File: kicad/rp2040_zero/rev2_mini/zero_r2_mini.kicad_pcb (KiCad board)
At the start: 2 copper layers, 34.6 x 28.3 mm, 15 parts, among them J3 Debug port, J5 Debug port, Q1 DMG2302U, U1 RP2040-Zero

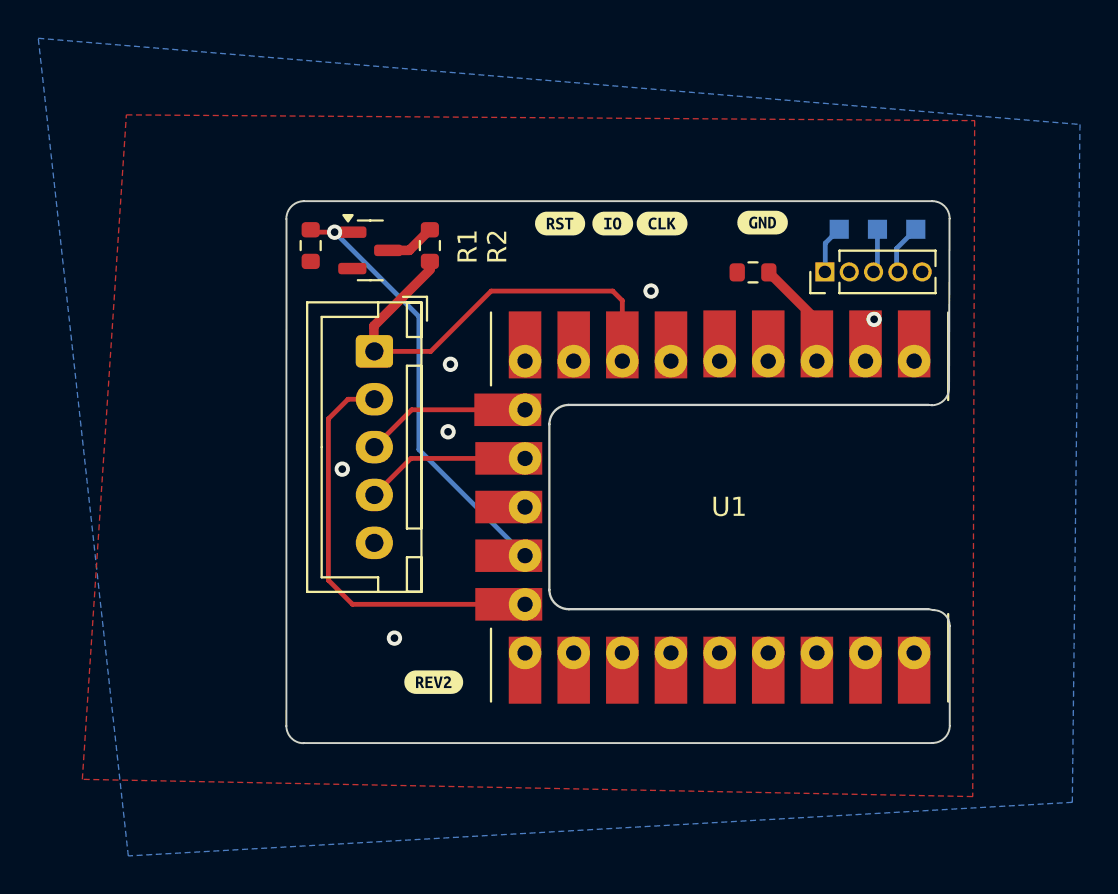
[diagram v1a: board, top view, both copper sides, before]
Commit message: kicad: add pullup resistor on rp2040
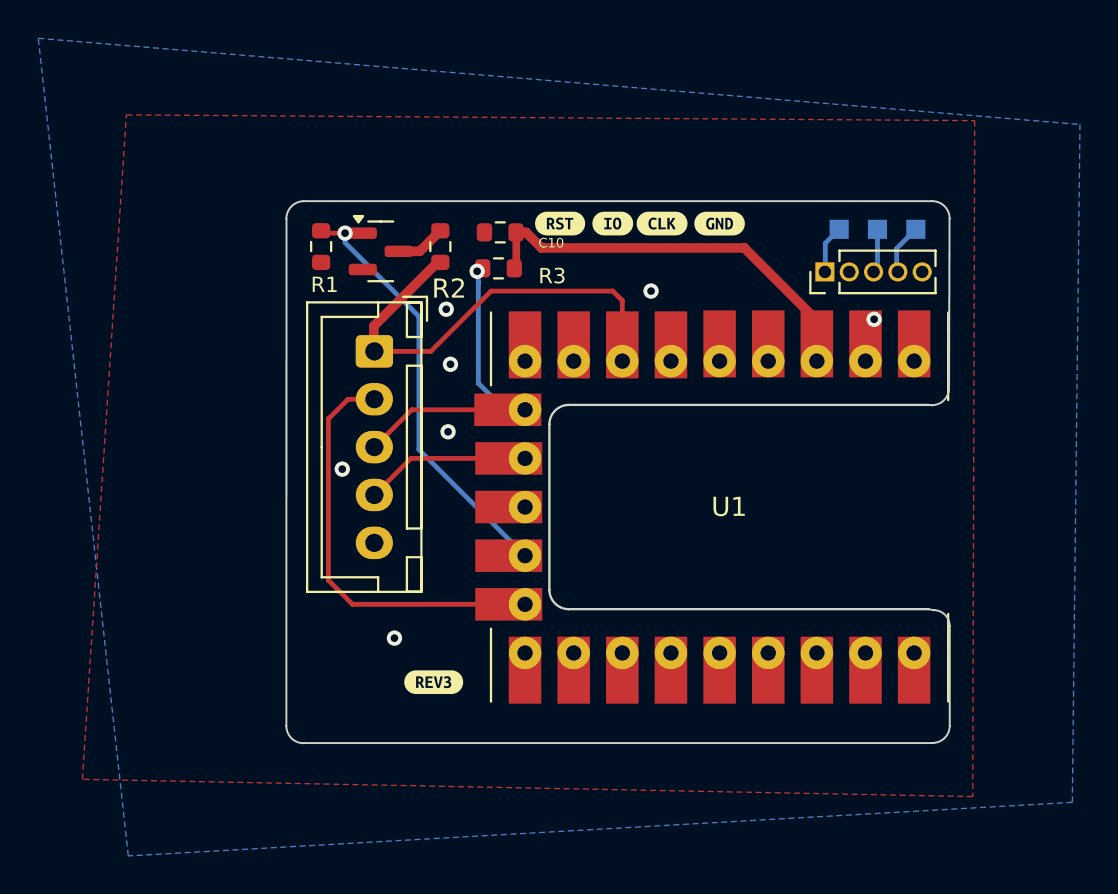
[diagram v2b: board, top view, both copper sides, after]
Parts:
- removed kibuzzard-6845954C: G***, kibuzzard-6845954C
- added R3: 1k, Resistor_SMD:R_0603_1608Metric, F.Cu at (126.5, 71.7)
- added kibuzzard-6AAE3AD3: G***, kibuzzard-6AAE3AD3, F.Cu at (123.2, 93.3)
- moved C10 13.4 mm to (126.6, 69.8)
- moved kibuzzard-67D71D53 2.25 mm to (138.1, 69.4)
- moved Q1 0.55 mm to (120.4, 70.8)
- moved R1 0.55 mm to (117.3, 70.6)
- moved R2 0.55 mm to (123.5, 70.6)
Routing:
- net +3.3V: track 3.55 -> 19.4 mm
- net OUT_SWDIO: track 8.68 -> 17.7 mm, vias 0 -> 1
- net INOUT_NRESET: track 22.2 -> 22.9 mm
- net GND: vias 6 -> 7
